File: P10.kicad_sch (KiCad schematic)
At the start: 59 parts

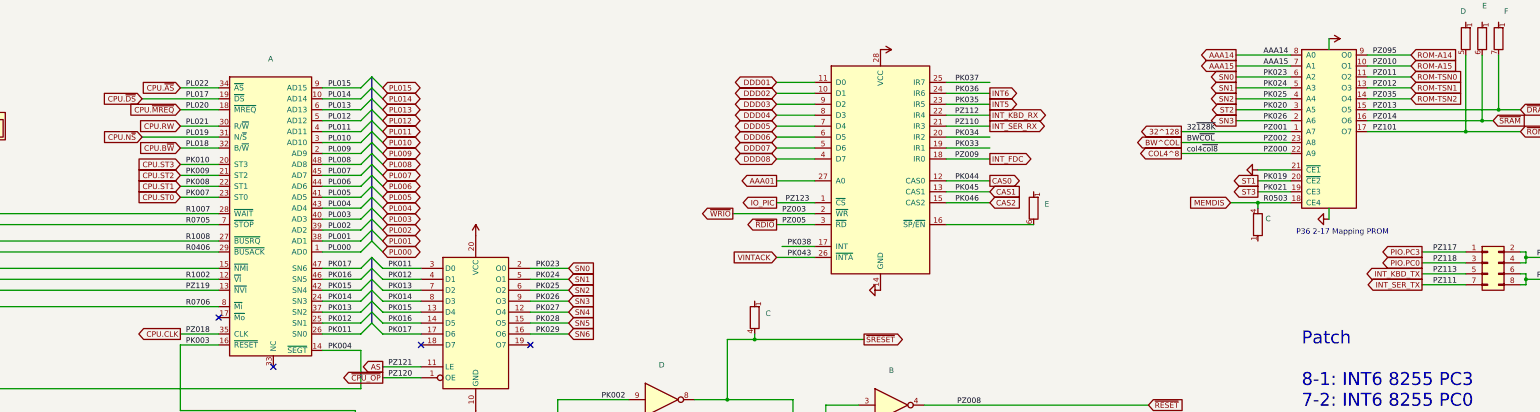
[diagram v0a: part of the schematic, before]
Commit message: fixing KiCad6 warnings
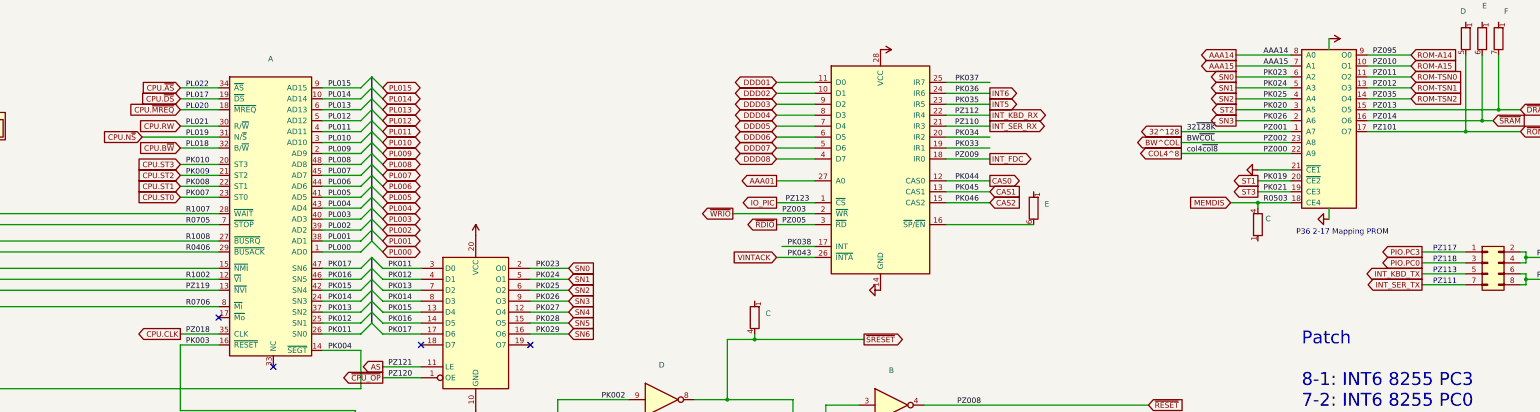
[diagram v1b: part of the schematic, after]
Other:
- note added: "PK009"
- note added: "PL017"
- note added: "PL020"
- note added: "PL022"
- note added: "PZ111"
- note added: "PZ113"
- note added: "PZ117"
- note added: "PZ118"
